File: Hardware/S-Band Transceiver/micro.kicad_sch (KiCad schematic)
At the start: 3 parts, among them J2 AVR-UPDI-6, U11 AVR128DA48x-xPT, U12 ADS1118IDGS

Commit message: Updates to schematic
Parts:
- added C32, C33, C34, C35, C36, C37: 100nF, symbol Device:C_Small
- added C38, C39: 47pF, symbol Device:C_Small
- added D1: SP0503BAHT, Package_TO_SOT_SMD:SOT-143, symbol Power_Protection:SP0503BAHT
- added J4: USB_C_Receptacle_USB2.0_16P, symbol Connector:USB_C_Receptacle_USB2.0_16P
- added R10, R11: 5.1k, symbol Device:R_Small_US
- added R12, R13: 27, symbol Device:R_Small_US
- added U8: FT231XQ, Package_DFN_QFN:QFN-20-1EP_4x4mm_P0.5mm_EP2.5x2.5mm, symbol Interface_USB:FT231XQ
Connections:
- net SCLK: now reaches U12.1 (SCLK)
- net SCLK: now also U11.2 (PA6)
- net MOSI: now reaches U12.10 (DIN)
- net MOSI: now also U11.48 (PA4)
- net ~{CS}: now reaches U12.2 (~{CS})
- net ~{CS}: now also U11.3 (PA7)
- net GND: now reaches U12.3 (GND)
- net GND: now also J2.6 (GND), U11.15 (GND), U11.29 (GND), U11.43 (GND), C32.2, C33.1, C34.1, C35.1, C36.2, C37.1, C38.2, C39.2, D1.1 (A), J4.A1 (GND), J4.A12 (GND), J4.B1 (GND), J4.B12 (GND), J4.S1 (SHIELD), R10.2, R11.2, U8.13 (GND), U8.21 (GND), U8.3 (GND)
- net +3V3: now reaches U12.8 (VDD)
- net +3V3: now also J2.2 (VCC), U11.14 (VDD), U11.28 (AVDD), U11.42 (VDD), C32.1, C33.2, C34.2, C36.1, C37.2, U8.10 (3V3OUT), U8.11 (~{RESET}), U8.20 (VCCIO)
- net MISO: now reaches U12.9 (DOUT/~{DRDY})
- net MISO: now also U11.1 (PA5)
- net UPDI: now reaches U11.41 (UPDI)
- net UPDI: now also J2.1 (DATA)
- net TX: now reaches U11.44 (PA0)
- net TX: now also U8.1 (RXD)
- net RX: now reaches U11.45 (PA1)
- net RX: now also U8.17 (TXD)
- new net: J4.A5 (CC1), R11.1
- new net: R13.2, U8.8 (USBDP)
- new net: J4.B5 (CC2), R10.1
- new net: R12.2, U8.9 (USBDM)
- new net USBDM: C38.1, D1.3 (K), J4.A7 (D-), J4.B7 (D-), R13.1
- new net USBDP: C39.1, D1.2 (K), J4.A6 (D+), J4.B6 (D+), R12.1
- new net VBUS: D1.4 (K), J4.A4 (VBUS), J4.A9 (VBUS), J4.B4 (VBUS), J4.B9 (VBUS)
- new net VBUS_FILT: C35.2, U8.12 (VCC)
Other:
- note added: "Defined from Microcontroller"
- moved on the sheet: J2, U11, U12

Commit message: Updating schematic
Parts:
- added C42, C43: 10uF, symbol Device:C_Polarized_Small_US
- added L6: L_Small, symbol Device:L_Small
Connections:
- net GND: now also C42.2, C43.2
- net VBUS: now also C42.1, L6.1
- net VBUS_FILT: now also C43.1, L6.2
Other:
- note added: "FTDI USB to UART"
- note added: "USB Connector"
- moved on the sheet: C32, C33, C34, D1, J2, J4, R10, R11, U11, U12

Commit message: Changes to schematic
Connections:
- net VBUS_FILT renamed +5V
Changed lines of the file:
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@@
 		)
 	)
-	(global_label "VBUS_FILT"
-		(shape input)
-		(at 229.87 95.25 90)
-		(fields_autoplaced yes)
-		(effects
-			(font
-				(size 1.27 1.27)
-			)
-			(justify left)
-		)
-		(property "Intersheetrefs" "${INTERSHEET_REFS}"
-			(at 229.87 82.7095 90)
-			(effects
-				(font
-					(size 1.27 1.27)
-				)
-				(justify left)
-				(hide yes)
-			)
-		)
-	)
 	(global_label "USBDP"
 		(shape input)
@@
 		)
 	)
-	(global_label "VBUS_FILT"
-		(shape input)
-		(at 267.97 29.21 90)
-		(fields_autoplaced yes)
-		(effects
-			(font
-				(size 1.27 1.27)
-			)
-			(justify left)
-		)
-		(property "Intersheetrefs" "${INTERSHEET_REFS}"
-			(at 267.97 16.6695 90)
-			(effects
-				(font
-					(size 1.27 1.27)
-				)
-				(justify left)
-				(hide yes)
-			)
-		)
-	)
 	(global_label "MISO"
 		(shape input)
@@
 	)
 	(symbol
+		(lib_id "power:+5V")
+		(at 267.97 29.21 0)
+		(unit 1)
+		(exclude_from_sim no)
+		(in_bom yes)
+		(on_board yes)
+		(dnp no)
+		(fields_autoplaced yes)
+		(property "Reference" "#PWR045"
+			(at 267.97 33.02 0)
+			(effects
+				(font
+					(size 1.27 1.27)
+				)
+				(hide yes)
+			)
+		)
+		(property "Value" "+5V"
+			(at 267.97 24.13 0)
+			(effects
+				(font
+					(size 1.27 1.27)
+				)
+			)
+		)
+		(property "Footprint" ""
+			(at 267.97 29.21 0)
+			(effects
+				(font
+					(size 1.27 1.27)
+				)
+				(hide yes)
+			)
+		)
+		(property "Datasheet" ""
+			(at 267.97 29.21 0)
+			(effects
+				(font
+					(size 1.27 1.27)
+				)
+				(hide yes)
+			)
+		)
+		(property "Description" "Power symbol creates a global label with name \"+5V\""
+			(at 267.97 29.21 0)
+			(effects
+				(font
+					(size 1.27 1.27)
+				)
+				(hide yes)
+			)
+		)
+		(pin "1"
+		)
+		(instances
+			(project "S-Band Transceiver"
+				(path "/811f57cf-e3df-4fba-aff9-353adc85299e/03e3241c-59a9-4f6f-b7cc-ae3fa2c59abc"
+					(reference "#PWR045")
+					(unit 1)
+				)
+			)
+		)
+	)
+	(symbol
 		(lib_id "Device:C_Small")
 		(at 226.06 100.33 90)
@@
 					(unit 1)
 				)
+			)
+		)
+	)
+	(symbol
+		(lib_id "power:+5V")
+		(at 229.87 95.25 0)
+		(unit 1)
+		(exclude_from_sim no)
+		(in_bom yes)
+		(on_board yes)
+		(dnp no)
+		(fields_autoplaced yes)
+		(property "Reference" "#PWR044"
+			(at 229.87 99.06 0)
+			(effects
+				(font
+					(size 1.27 1.27)
+				)
+				(hide yes)
+			)
+		)
+		(property "Value" "+5V"
+			(at 229.87 90.17 0)
+			(effects
+				(font
+					(size 1.27 1.27)
+				)
+			)
+		)
+		(property "Footprint" ""
+			(at 229.87 95.25 0)
+			(effects
+				(font
+					(size 1.27 1.27)
+				)
+				(hide yes)
+			)
+		)
+		(property "Datasheet" ""
+			(at 229.87 95.25 0)
+			(effects
+				(font
+					(size 1.27 1.27)
+				)
+				(hide yes)
+			)
+		)
+		(property "Description" "Power symbol creates a global label with name \"+5V\""
+			(at 229.87 95.25 0)
+			(effects
+				(font
+					(size 1.27 1.27)
+				)
+				(hide yes)
+			)
+		)
+		(pin "1"
+		)
+		(instances
+			(project "S-Band Transceiver"
+				(path "/811f57cf-e3df-4fba-aff9-353adc85299e/03e3241c-59a9-4f6f-b7cc-ae3fa2c59abc"
+					(reference "#PWR044")
+					(unit 1)
+				)

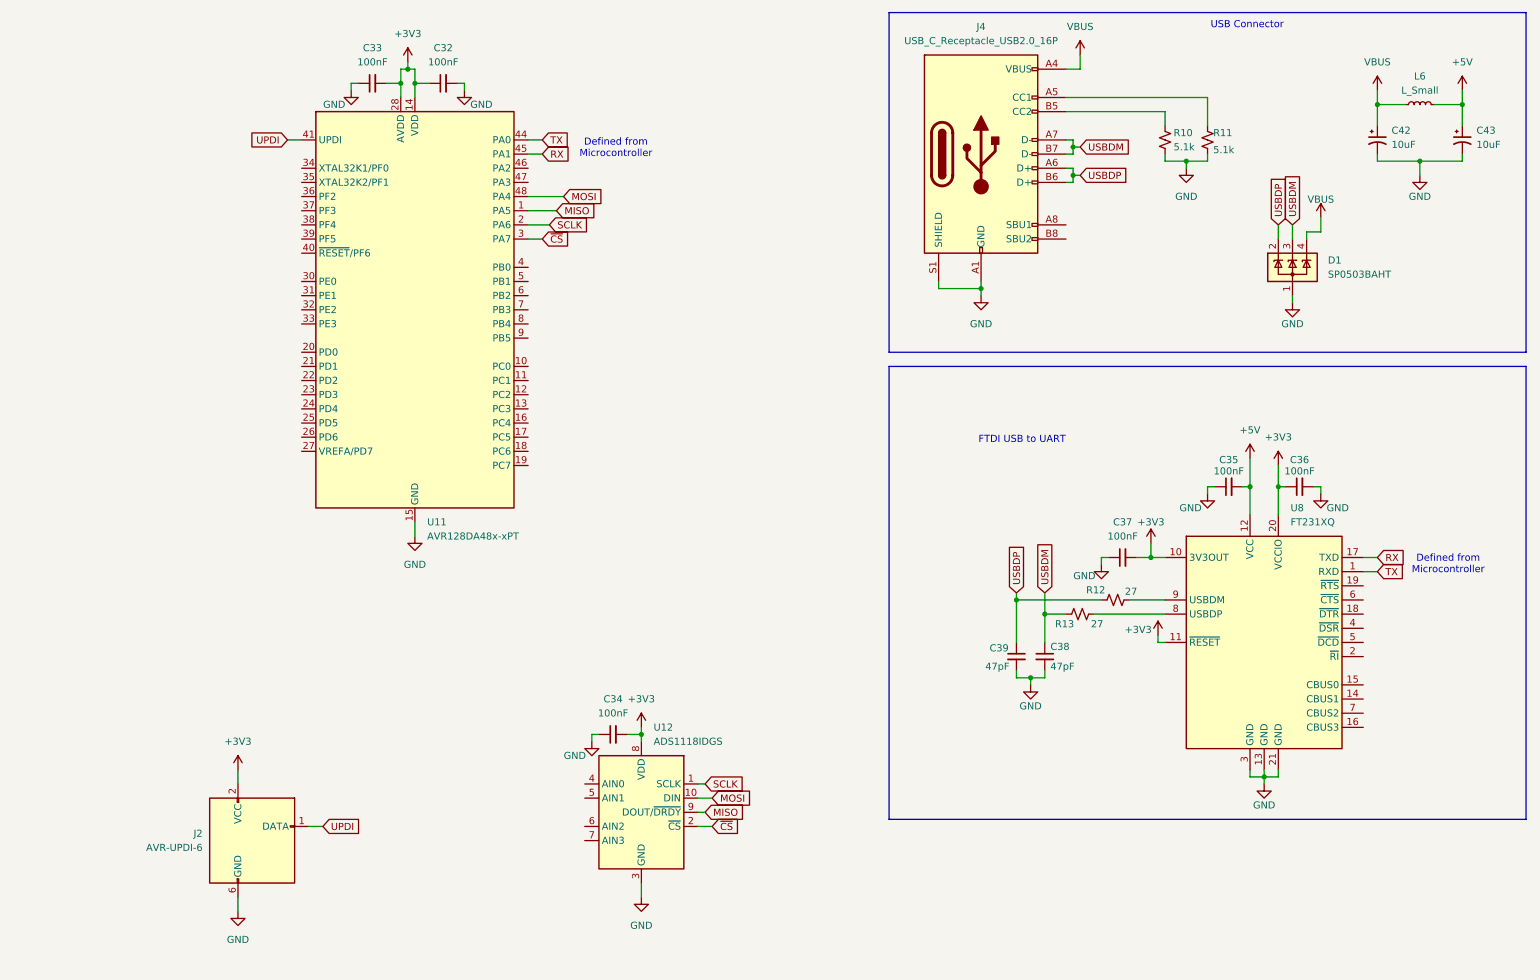
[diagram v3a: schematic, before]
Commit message: Updating microcontroller schematic
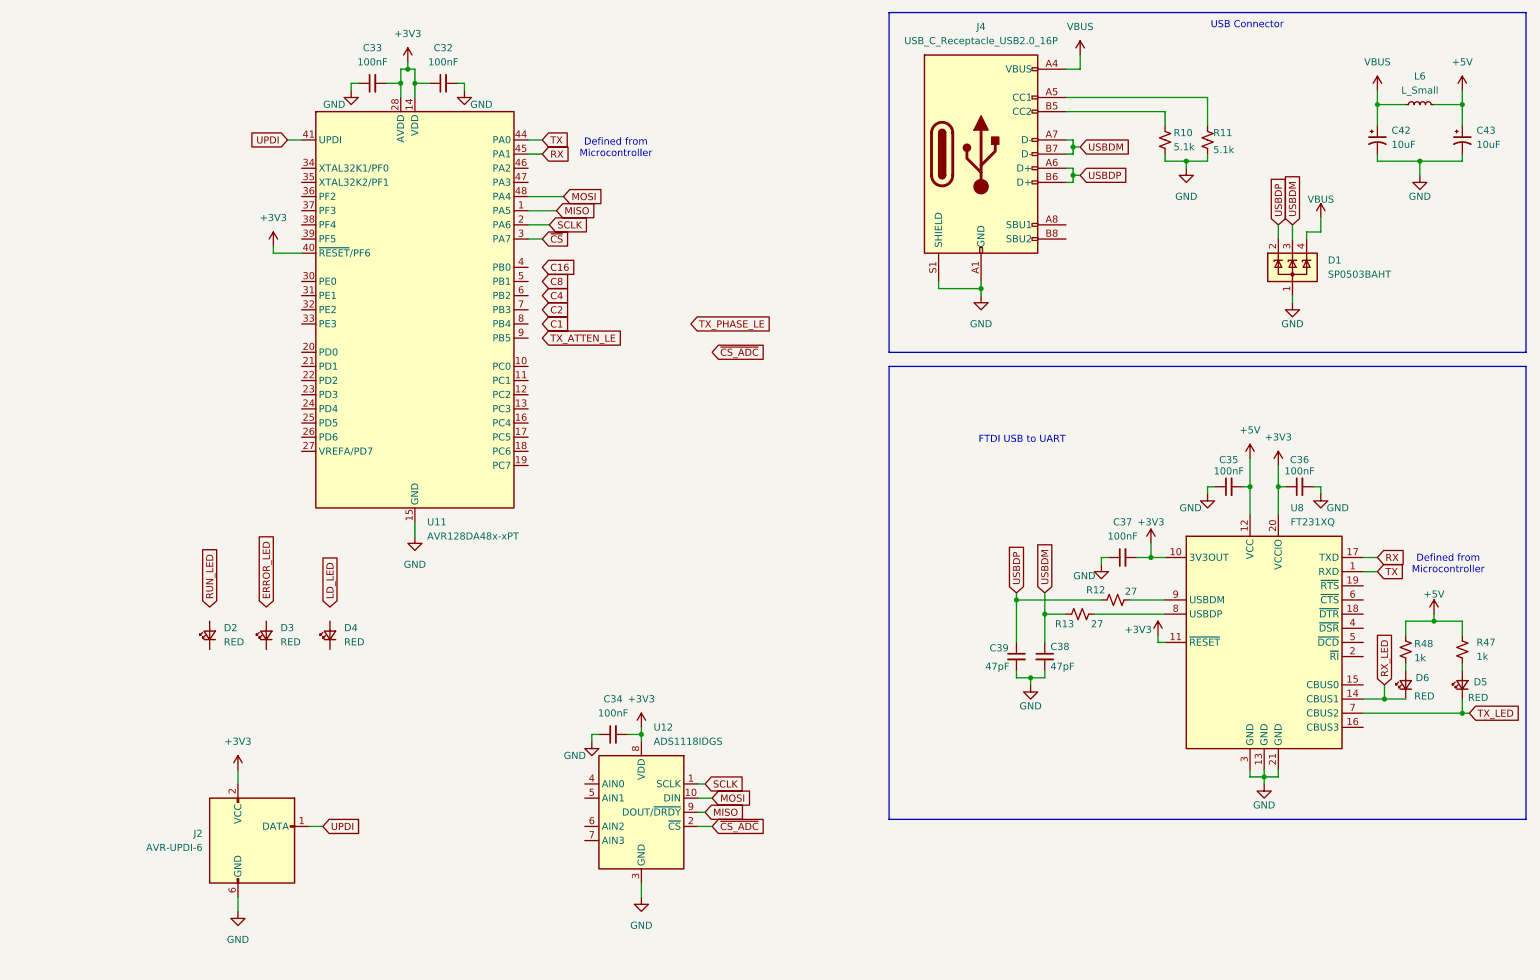
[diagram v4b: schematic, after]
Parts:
- added D2, D3, D4, D5, D6: RED, symbol Device:LED_Small
- added R47, R48: 1k, symbol Device:R_Small_US
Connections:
- net +3V3: now also U11.40 (~{RESET}/PF6)
- net +5V: now also R47.1, R48.1
- net ~{CS}: no longer U12.2 (~{CS})
- net RX_LED: now reaches U8.14 (CBUS1)
- net RX_LED: now also D6.1 (K)
- net TX_LED: now reaches U8.7 (CBUS2)
- net TX_LED: now also D5.1 (K)
- new net: D6.2 (A), R48.2
- new net: D5.2 (A), R47.2
- new net ~{CS_ADC}: U12.2 (~{CS})

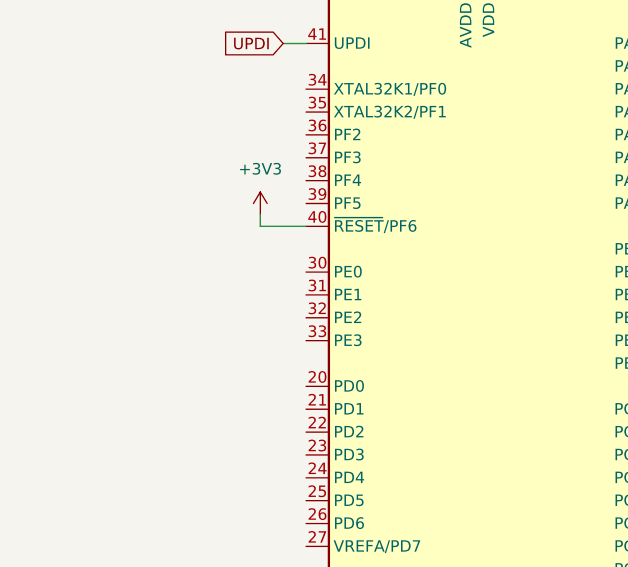
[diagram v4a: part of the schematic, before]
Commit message: Updating PLL
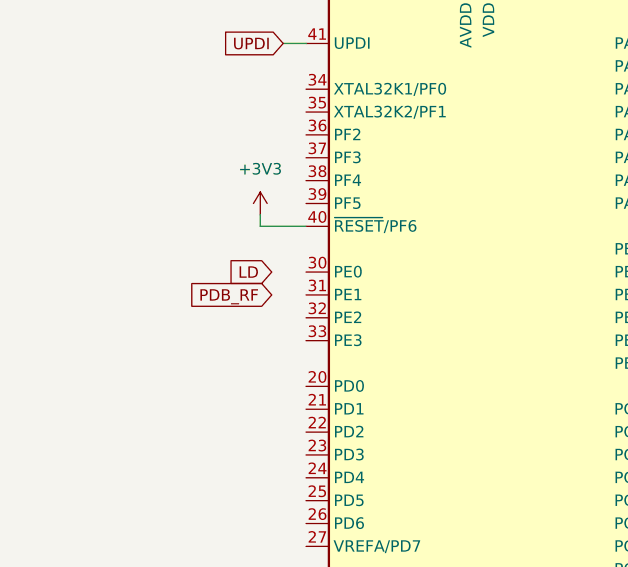
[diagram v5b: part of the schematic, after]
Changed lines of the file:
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@@
+		)
+	)
+	(global_label "PDB_RF"
+		(shape input)
+		(at 55.88 66.04 180)
+		(fields_autoplaced yes)
+		(effects
+			(font
+				(size 1.27 1.27)
+			)
+			(justify right)
+		)
+		(property "Intersheetrefs" "${INTERSHEET_REFS}"
+			(at 45.7586 66.04 0)
+			(effects
+				(font
+					(size 1.27 1.27)
+				)
+				(justify right)
+				(hide yes)
+			)
 		)
 	)
@@
 				(hide yes)
 			)
+		)
+	)
+	(global_label "LD"
+		(shape input)
+		(at 55.88 63.5 180)
+		(fields_autoplaced yes)
+		(effects
+			(font
+				(size 1.27 1.27)
+			)
+			(justify right)
+		)
+		(property "Intersheetrefs" "${INTERSHEET_REFS}"
+			(at 50.5967 63.5 0)
+			(effects
+				(font
+					(size 1.27 1.27)
+				)
+				(justify right)
+				(hide yes)
+			)

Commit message: Updates to schematic
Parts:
- added C86, C87: 10nF, symbol Device:C_Small
- added R52, R53, R54, R57, R58: 1k, symbol Device:R_Small_US
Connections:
- net +5V: now also R52.1
- net GND: now also D2.1 (K), D3.1 (K), D4.1 (K), C86.2, C87.2
- net at D3.2 (A): now also R53.2
- net at U12.4 (AIN0): now also C87.1, R57.2
- net at U12.5 (AIN1): now also C86.1, R58.2
- net at D2.2 (A): now also R54.2
- net at D4.2 (A): now also R52.2
- new net RX_VRMS: R58.1
- new net TX_VRMS: R57.1

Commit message: Updates to schematic
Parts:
- added C88: 100nF, symbol Device:C_Small
- added C89, C90: 10nF, symbol Device:C_Small
- added R61: 1k, symbol Device:R_Small_US
- added SW1: SW_Push, symbol Switch:SW_Push
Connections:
- net +3V3: now also C89.1, C90.2; no longer U11.40 (~{RESET}/PF6)
- net ERROR_LED: now also R53.1
- net GND: now also C88.1, C89.2, C90.1, SW1.1
- net RUN_LED: now also R54.1
- new net: R61.1, SW1.2
- new net: C88.2, R61.2, U11.40 (~{RESET}/PF6)
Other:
- moved on the sheet: C32, C33
